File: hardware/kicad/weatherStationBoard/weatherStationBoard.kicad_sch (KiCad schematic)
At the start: 7 parts, among them P1 USB_C_Plug_USB2.0, SW1 SW_Push, SW2 SW_Push, U1 ESP-12F, U2 AMS1117, U3 CH340C

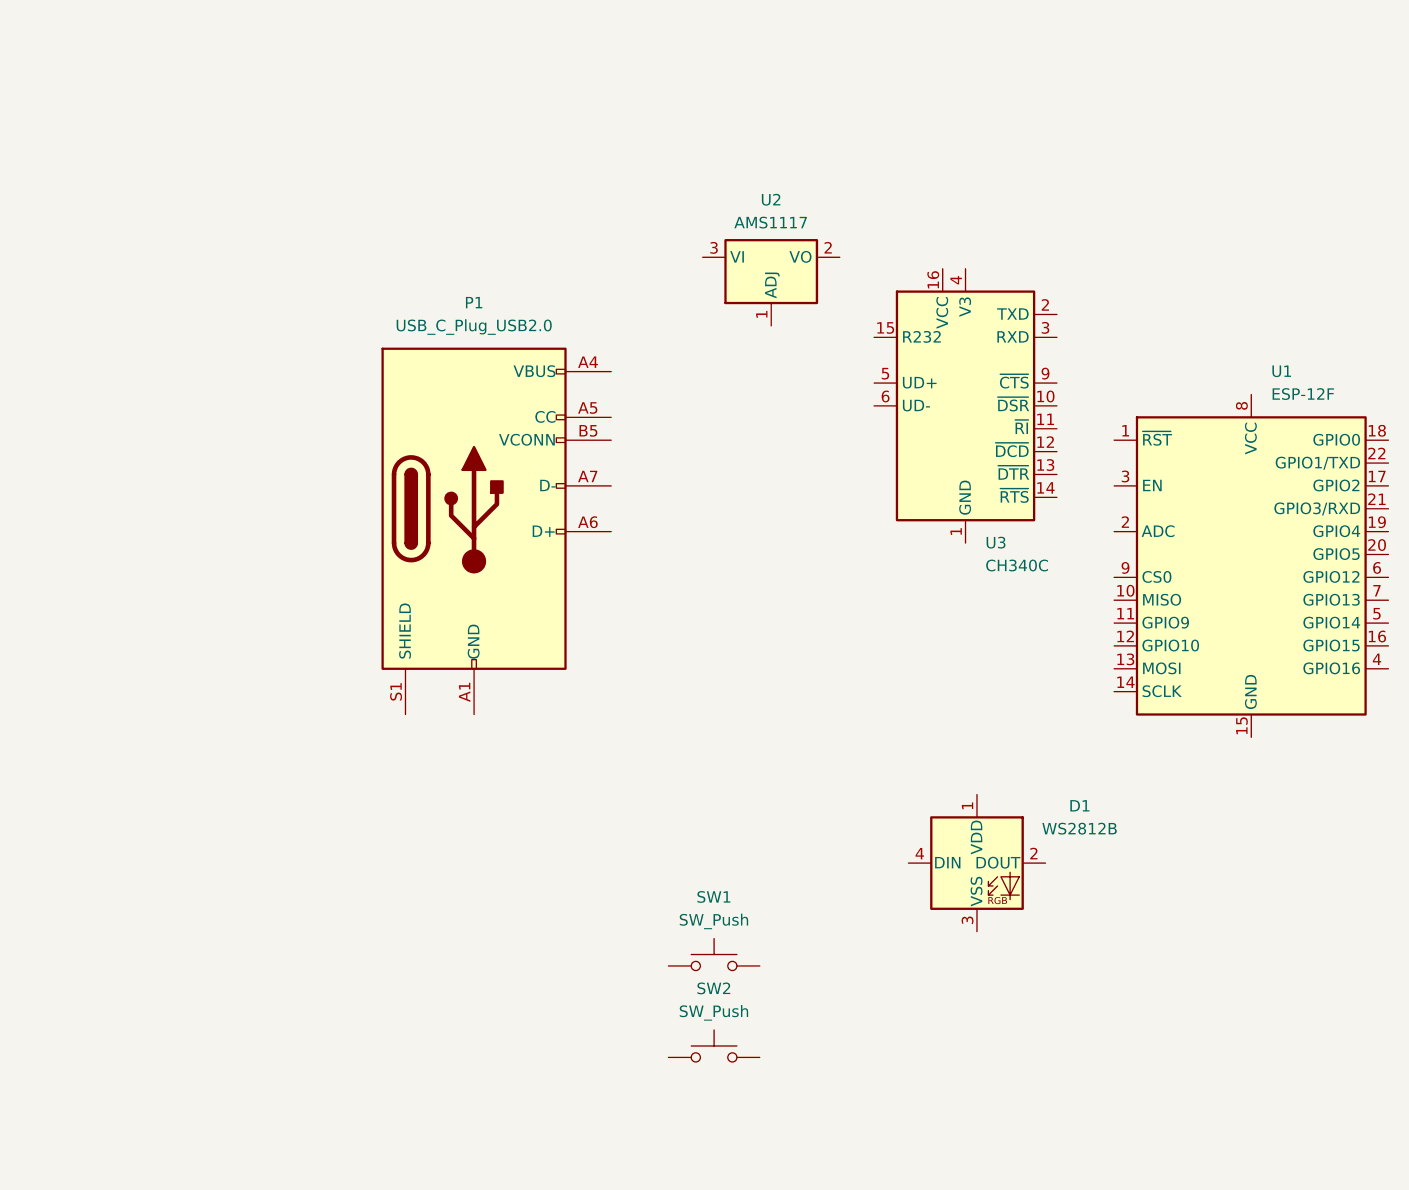
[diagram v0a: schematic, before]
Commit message: PCB Simple LED Circuit With Usb-C
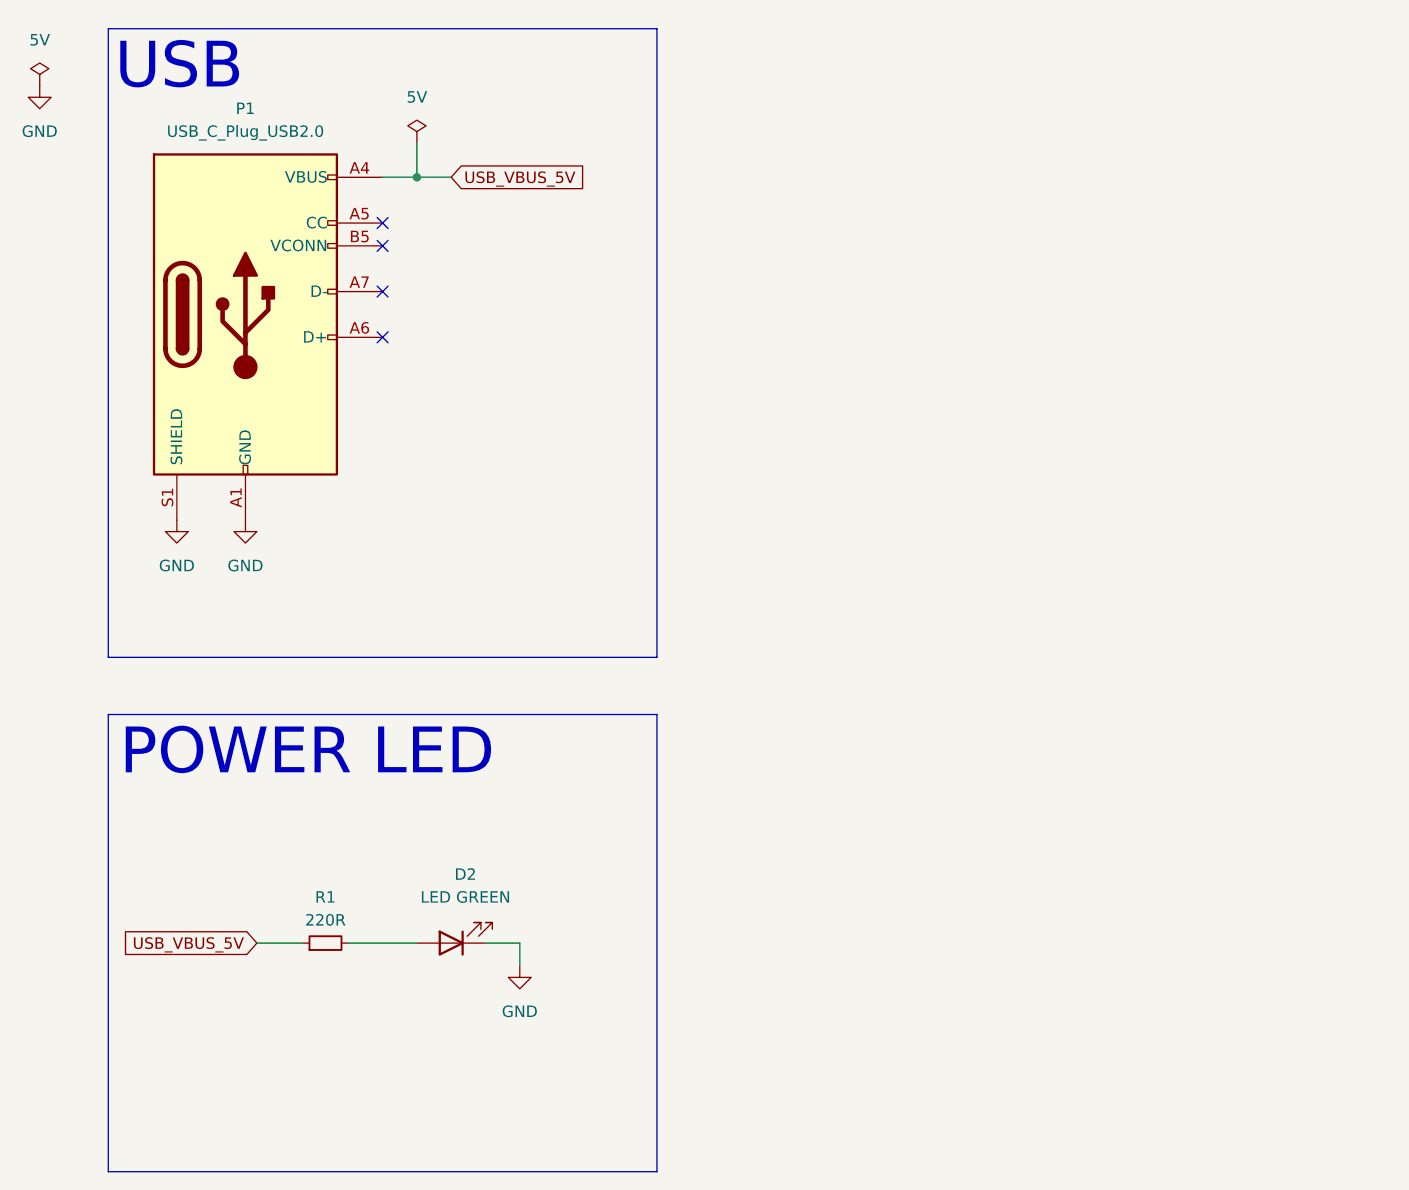
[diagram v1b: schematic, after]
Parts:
- removed D1: WS2812B, LED_SMD:LED_WS2812B_PLCC4_5.0x5.0mm_P3.2mm, symbol LED:WS2812B
- removed SW1, SW2: SW_Push, symbol Switch:SW_Push
- removed U1: ESP-12F, RF_Module:ESP-12E, symbol RF_Module:ESP-12F
- removed U2: AMS1117, Package_TO_SOT_SMD:SOT-223-3_TabPin2, symbol Regulator_Linear:AMS1117
- removed U3: CH340C, Package_SO:SOIC-16_3.9x9.9mm_P1.27mm, symbol Interface_USB:CH340C
- added D2: LED GREEN, LED_SMD:LED_0805_2012Metric, symbol Device:LED
- added R1: 220R, Resistor_SMD:R_0805_2012Metric, symbol Device:R_Small
- P1: footprint (none) -> Connector_USB:USB_C_Receptacle_GCT_USB4085
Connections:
- net GND: now reaches P1.A1 (GND), P1.A12 (GND), P1.B1 (GND), P1.B12 (GND)
- net GND: now also P1.S1 (SHIELD), D2.1 (K)
- net USB_VBUS_5V: now reaches P1.A4 (VBUS), P1.A9 (VBUS), P1.B4 (VBUS), P1.B9 (VBUS)
- net USB_VBUS_5V: now also R1.1
- new net: D2.2 (A), R1.2
- no-connect marks 0 -> 4
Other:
- note added: "POWER LED"
- note added: "USB"
- moved on the sheet: P1

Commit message: power, 5vto3v, usb to serial
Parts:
- added 12k1: R_Small, Resistor_SMD:R_0805_2012Metric, symbol Device:R_Small
- added C1, C10, C5, C6, C8: 100nF, Capacitor_SMD:C_0805_2012Metric, symbol Device:C_Small
- added C2, C7, C9: 10uF, Capacitor_SMD:C_0805_2012Metric, symbol Device:C_Small
- added C3, C4: 22pF, Capacitor_SMD:C_0805_2012Metric, symbol Device:C_Small
- added D1: LED, LED_SMD:LED_0805_2012Metric, symbol Device:LED_Small
- added Q1, Q2: S8050, Package_TO_SOT_THT:TO-92_Inline, symbol Transistor_BJT:S8050
- added R2, R3: 470R, Resistor_SMD:R_0805_2012Metric, symbol Device:R_Small
- added R4: 1k, Resistor_SMD:R_0805_2012Metric, symbol Device:R_Small
- added R5: 12k, Resistor_SMD:R_0805_2012Metric, symbol Device:R_Small
- added U1: ESP-12F, RF_Module:ESP-12E, symbol RF_Module:ESP-12F
- added U2: CH340G, Package_SO:SOIC-16_3.9x9.9mm_P1.27mm, symbol Interface_USB:CH340G
- added U4: AMS1117-3.3, Package_TO_SOT_SMD:SOT-223-3_TabPin2, symbol Regulator_Linear:AMS1117-3.3
- added Y1: Crystal_GND24_Small, Crystal:Crystal_SMD_3225-4Pin_3.2x2.5mm, symbol Device:Crystal_GND24_Small
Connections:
- net GND: now also C1.2, C10.2, C2.2, C3.2, C4.2, C5.2, C6.2, C7.2, C8.2, C9.2, D1.1 (K), U1.15 (GND), U2.1 (GND), U4.1 (GND), Y1.2, Y1.4
- net at P1.A6 (D+): now also U2.5 (UD+)
- net at P1.A7 (D-): now also U2.6 (UD-)
- net USB_VBUS_5V renamed 5V
- net 5V: now also C1.1, C2.1, C6.1, C7.1, U2.16 (VCC), U4.3 (VI)
- new net: R3.1, U2.3 (RXD)
- new net: D1.2 (A), R4.2
- new net: 12k1.1, Q2.2 (B)
- new net: R2.1, U2.2 (TXD)
- new net: Q1.2 (B), R5.1
- new net: C10.1, U2.4 (V3)
- new net 3V3: C5.1, C8.1, C9.1, R4.1, U1.8 (VCC), U4.2 (VO)
- new net DTR: 12k1.2, Q1.1 (E), U2.13 (~{DTR})
- new net ESP RX: R2.2, U1.21 (GPIO3/RXD)
- new net ESP TX: R3.2, U1.22 (GPIO1/TXD)
- new net GPIO0: Q1.3 (C), U1.18 (GPIO0)
- new net RTS: Q2.1 (E), R5.2, U2.14 (~{RTS})
- new net XI: C4.1, U2.7 (XI), Y1.3
- new net XO: C3.1, U2.8 (XO), Y1.1
- new net nRST: Q2.3 (C), U1.1 (~{RST})
- no-connect marks 4 -> 23
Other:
- note added: "5V 2 3V"
- note added: "Auto program circuit"
- note added: "ESP8266"
- moved on the sheet: D2, R1

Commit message: PCB updated
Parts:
- added R6: 5k1, Resistor_SMD:R_0805_2012Metric, symbol Device:R_Small
- Q1, Q2: footprint Package_TO_SOT_THT:TO-92_Inline -> Package_TO_SOT_SMD:SOT-23-3
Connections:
- net GND: now also R6.2
- net at P1.A5 (CC): now also R6.1
- no-connect marks 23 -> 22
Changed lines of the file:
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@@
 	)
 	(no_connect
-		(at 43.18 34.29)
-	)
-	(no_connect
 		(at 175.26 45.72)
 	)
@@
 	(wire
 		(pts
+			(xy 43.18 34.29) (xy 45.72 34.29)
+		)
+		(stroke
+			(width 0)
+			(type default)
+		)
+	)
+	(wire
+		(pts
 			(xy 63.5 57.15) (xy 66.04 57.15)
 		)
@@
 	(wire
 		(pts
+			(xy 50.8 34.29) (xy 53.34 34.29)
+		)
+		(stroke
+			(width 0)
+			(type default)
+		)
+	)
+	(wire
+		(pts
 			(xy 212.09 31.75) (xy 218.44 31.75)
 		)
@@
 	)
 	(symbol
+		(lib_id "Device:R_Small")
+		(at 48.26 34.29 90)
+		(unit 1)
+		(exclude_from_sim no)
+		(in_bom yes)
+		(on_board yes)
+		(dnp no)
+		(property "Reference" "R6"
+			(at 55.626 34.544 90)
+			(effects
+				(font
+					(size 1.27 1.27)
+				)
+			)
+		)
+		(property "Value" "5k1"
+			(at 48.26 36.83 90)
+			(effects
+				(font
+					(size 1.27 1.27)
+				)
+			)
+		)
+		(property "Footprint" "Resistor_SMD:R_0805_2012Metric"
+			(at 48.26 34.29 0)
+			(effects
+				(font
+					(size 1.27 1.27)
+				)
+				(hide yes)
+			)
+		)
+		(property "Datasheet" "~"
+			(at 48.26 34.29 0)
+			(effects
+				(font
+					(size 1.27 1.27)
+				)
+				(hide yes)
+			)
+		)
+		(property "Description" "Resistor, small symbol"
+			(at 48.26 34.29 0)
+			(effects
+				(font
+					(size 1.27 1.27)
+				)
+				(hide yes)
+			)
+		)
+		(pin "2"
+		)
+		(pin "1"
+		)
+		(instances
+			(project "weatherStationBoard"
+				(path "/8b822046-1d25-4aa8-8dbc-df598e1eff63"
+					(reference "R6")
+					(unit 1)
+				)
+			)
+		)
+	)
+	(symbol
 		(lib_id "power:GND")
 		(at 252.73 38.1 0)
@@
 			)
 		)
-		(property "Footprint" "Package_TO_SOT_THT:TO-92_Inline"
+		(property "Footprint" "Package_TO_SOT_SMD:SOT-23-3"
 			(at 73.66 102.235 0)
 			(effects
@@
 	)
 	(symbol
+		(lib_id "power:GND")
+		(at 53.34 34.29 0)
+		(unit 1)
+		(exclude_from_sim no)
+		(in_bom yes)
+		(on_board yes)
+		(dnp no)
+		(fields_autoplaced yes)
+		(property "Reference" "#PWR020"
+			(at 53.34 40.64 0)
+			(effects
+				(font
+					(size 1.27 1.27)
+				)
+				(hide yes)
+			)
+		)
+		(property "Value" "GND"
+			(at 53.34 39.37 0)
+			(effects
+				(font
+					(size 1.27 1.27)
+				)
+			)
+		)
+		(property "Footprint" ""
+			(at 53.34 34.29 0)
+			(effects
+				(font
+					(size 1.27 1.27)
+				)
+				(hide yes)
+			)
+		)
+		(property "Datasheet" ""
+			(at 53.34 34.29 0)
+			(effects
+				(font
+					(size 1.27 1.27)
+				)
+				(hide yes)
+			)
+		)
+		(property "Description" "Power symbol creates a global label with name \"GND\" , ground"
+			(at 53.34 34.29 0)
+			(effects
+				(font
+					(size 1.27 1.27)
+				)
+				(hide yes)
+			)
+		)
+		(pin "1"
+		)
+		(instances
+			(project "weatherStationBoard"
+				(path "/8b822046-1d25-4aa8-8dbc-df598e1eff63"
+					(reference "#PWR020")
+					(unit 1)
+				)
+			)
+		)
+	)
+	(symbol
 		(lib_id "Device:R_Small")
 		(at 91.44 115.57 90)
@@
 			)
 		)
-		(property "Footprint" "Package_TO_SOT_THT:TO-92_Inline"
+		(property "Footprint" "Package_TO_SOT_SMD:SOT-23-3"
 			(at 73.66 113.665 0)
 			(effects

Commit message: Pushbutton files
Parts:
- added R7: 10k, Resistor_SMD:R_0805_2012Metric, symbol Device:R_Small
- added SW1: SW_Push, symbol Switch:SW_Push
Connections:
- net 3V3: now also R7.2
- net nRST: now also R7.1, SW1.1
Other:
- note added: "RESET"
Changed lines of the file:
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@@
 	(generator "eeschema")
 	(generator_version "8.0")
-	(paper "A4")
+	(paper "A3")
 	(junction
 		(at 63.5 29.21)
@@
 	)
 	(junction
+		(at 134.62 109.22)
+		(diameter 0)
+		(color 0 0 0 0)
+	)
+	(junction
 		(at 252.73 24.13)
 		(diameter 0)
@@
 	(wire
 		(pts
+			(xy 134.62 106.68) (xy 134.62 109.22)
+		)
+		(stroke
+			(width 0)
+			(type default)
+		)
+	)
+	(wire
+		(pts
 			(xy 63.5 29.21) (xy 68.58 29.21)
 		)
@@
 	(wire
 		(pts
+			(xy 134.62 109.22) (xy 140.97 109.22)
+		)
+		(stroke
+			(width 0)
+			(type default)
+		)
+	)
+	(wire
+		(pts
+			(xy 134.62 97.79) (xy 134.62 101.6)
+		)
+		(stroke
+			(width 0)
+			(type default)
+		)
+	)
+	(wire
+		(pts
 			(xy 252.73 36.83) (xy 252.73 38.1)
 		)
@@
 	(wire
 		(pts
+			(xy 134.62 109.22) (xy 134.62 113.03)
+		)
+		(stroke
+			(width 0)
+			(type default)
+		)
+	)
+	(wire
+		(pts
 			(xy 45.72 68.58) (xy 45.72 63.5)
 		)
@@
 	)
 	(rectangle
+		(start 120.65 83.82)
+		(end 172.72 134.62)
+		(stroke
+			(width 0)
+			(type default)
+		)
+		(fill
+			(type none)
+		)
+	)
+	(rectangle
 		(start 59.69 83.82)
 		(end 118.11 134.62)
@@
 		)
 	)
+	(text "RESET\n"
+		(exclude_from_sim no)
+		(at 132.588 88.392 0)
+		(effects
+			(font
+				(size 5.08 5.08)
+			)
+		)
+	)
 	(text "ESP8266"
 		(exclude_from_sim no)
@@
 		)
 	)
+	(label "nRST"
+		(at 140.97 109.22 0)
+		(fields_autoplaced yes)
+		(effects
+			(font
+				(size 1.27 1.27)
+			)
+			(justify left bottom)
+		)
+	)
 	(label "ESP TX"
 		(at 184.15 35.56 0)
@@
 	(global_label "3V3"
 		(shape input)
+		(at 134.62 97.79 90)
+		(fields_autoplaced yes)
+		(effects
+			(font
+				(size 1.27 1.27)
+			)
+			(justify left)
+		)
+		(property "Intersheetrefs" "${INTERSHEET_REFS}"
+			(at 134.62 91.2972 90)
+			(effects
+				(font
+					(size 1.27 1.27)
+				)
+				(justify left)
+				(hide yes)
+			)
+		)
+	)
+	(global_label "3V3"
+		(shape input)
 		(at 262.89 24.13 0)
 		(fields_autoplaced yes)
@@
 	)
 	(symbol
+		(lib_id "Switch:SW_Push")
+		(at 134.62 118.11 270)
+		(unit 1)
+		(exclude_from_sim no)
+		(in_bom yes)
+		(on_board yes)
+		(dnp no)
+		(fields_autoplaced yes)
+		(property "Reference" "SW1"
+			(at 138.43 116.8399 90)
+			(effects
+				(font
+					(size 1.27 1.27)
+				)
+				(justify left)
+			)
+		)
+		(property "Value" "SW_Push"
+			(at 138.43 119.3799 90)
+			(effects
+				(font
+					(size 1.27 1.27)
+				)
+				(justify left)
+			)
+		)
+		(property "Footprint" ""
+			(at 139.7 118.11 0)
+			(effects
+				(font
+					(size 1.27 1.27)
+				)
+				(hide yes)
+			)
+		)
+		(property "Datasheet" "~"
+			(at 139.7 118.11 0)
+			(effects
+				(font
+					(size 1.27 1.27)
+				)
+				(hide yes)
+			)
+		)
+		(property "Description" "Push button switch, generic, two pins"
+			(at 134.62 118.11 0)
+			(effects
+				(font
+					(size 1.27 1.27)
+				)
+				(hide yes)
+			)
+		)
+		(pin "1"
+		)
+		(pin "2"
+		)
+		(instances
+			(project ""
+				(path "/8b822046-1d25-4aa8-8dbc-df598e1eff63"
+					(reference "SW1")
+					(unit 1)
+				)
+			)
+		)
+	)
+	(symbol
 		(lib_id "power:GND")
 		(at 236.22 38.1 0)
@@
 					(unit 1)
 				)
+			)
+		)
+	)
+	(symbol
+		(lib_id "Device:R_Small")
+		(at 134.62 104.14 180)
+		(unit 1)
+		(exclude_from_sim no)
+		(in_bom yes)
+		(on_board yes)
+		(dnp no)
+		(property "Reference" "R7"
+			(at 130.81 103.378 0)
+			(effects
+				(font
+					(size 1.27 1.27)
+				)
+			)
+		)
+		(property "Value" "10k"
+			(at 130.81 105.918 0)
+			(effects
+				(font
+					(size 1.27 1.27)
+				)
+			)
+		)
+		(property "Footprint" "Resistor_SMD:R_0805_2012Metric"
+			(at 134.62 104.14 0)
+			(effects
+				(font
+					(size 1.27 1.27)
+				)
+				(hide yes)
+			)
+		)
+		(property "Datasheet" "~"
+			(at 134.62 104.14 0)
+			(effects
+				(font
+					(size 1.27 1.27)
+				)
+				(hide yes)
+			)
+		)
+		(property "Description" "Resistor, small symbol"
+			(at 134.62 104.14 0)
+			(effects
+				(font
+					(size 1.27 1.27)
+				)
+				(hide yes)
+			)
+		)
+		(pin "1"
+		)
+		(pin "2"
+		)
+		(instances
+			(project "weatherStationBoard"
+				(path "/8b822046-1d25-4aa8-8dbc-df598e1eff63"
+					(reference "R7")
+					(unit 1)
+				)

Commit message: Updated usb connector
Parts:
- added S1: PTS645SM43SMTR92LFS, PTS645SM43SMTR92LFS:PTS645_SMT_, symbol PTS645SM43SMTR92LFS:PTS645SM43SMTR92LFS
- P1: footprint Connector_USB:USB_C_Receptacle_GCT_USB4085 -> Connector_USB:USB_C_Receptacle_XKB_U262-16XN-4BVC11
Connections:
- no-connect marks 22 -> 27
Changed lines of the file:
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@@
+	)
+	(no_connect
+		(at 134.62 123.19)
+	)
+	(no_connect
+		(at 148.59 121.92)
 	)
 	(no_connect
@@
 	)
 	(no_connect
+		(at 148.59 124.46)
+	)
+	(no_connect
 		(at 144.78 48.26)
 	)
@@
 	)
 	(no_connect
+		(at 168.91 121.92)
+	)
+	(no_connect
 		(at 144.78 38.1)
 	)
@@
 	(no_connect
 		(at 144.78 53.34)
+	)
+	(no_connect
+		(at 168.91 124.46)
 	)
 	(no_connect
@@
 	)
 	(symbol
+		(lib_id "PTS645SM43SMTR92LFS:PTS645SM43SMTR92LFS")
+		(at 148.59 121.92 0)
+		(unit 1)
+		(exclude_from_sim no)
+		(in_bom yes)
+		(on_board yes)
+		(dnp no)
+		(fields_autoplaced yes)
+		(property "Reference" "S1"
+			(at 158.75 114.3 0)
+			(effects
+				(font
+					(size 1.27 1.27)
+				)
+			)
+		)
+		(property "Value" "PTS645SM43SMTR92LFS"
+			(at 158.75 116.84 0)
+			(effects
+				(font
+					(size 1.27 1.27)
+				)
+			)
+		)
+		(property "Footprint" "PTS645SM43SMTR92LFS:PTS645_SMT_"
+			(at 165.1 119.38 0)
+			(effects
+				(font
+					(size 1.27 1.27)
+				)
+				(justify left)
+				(hide yes)
+			)
+		)
+		(property "Datasheet" "https://www.ckswitches.com/media/1471/pts645.pdf"
+			(at 165.1 121.92 0)
+			(effects
+				(font
+					(size 1.27 1.27)
+				)
+				(justify left)
+				(hide yes)
+			)
+		)
+		(property "Description" "C & K COMPONENTS - PTS645SM43SMTR92LFS - SWITCH, SPST, 0.05A, 12VDC, SMD, 4.3MM"
+			(at 148.59 121.92 0)
+			(effects
+				(font
+					(size 1.27 1.27)
+				)
+				(hide yes)
+			)
+		)
+		(property "Description_1" "C & K COMPONENTS - PTS645SM43SMTR92LFS - SWITCH, SPST, 0.05A, 12VDC, SMD, 4.3MM"
+			(at 165.1 124.46 0)
+			(effects
+				(font
+					(size 1.27 1.27)
+				)
+				(justify left)
+				(hide yes)
+			)
+		)
+		(property "Height" ""
+			(at 165.1 127 0)
+			(effects
+				(font
+					(size 1.27 1.27)
+				)
+				(justify left)
+				(hide yes)
+			)
+		)
+		(property "Manufacturer_Name" "C & K COMPONENTS"
+			(at 165.1 129.54 0)
+			(effects
+				(font
+					(size 1.27 1.27)
+				)
+				(justify left)
+				(hide yes)
+			)
+		)
+		(property "Manufacturer_Part_Number" "PTS645SM43SMTR92LFS"
+			(at 165.1 132.08 0)
+			(effects
+				(font
+					(size 1.27 1.27)
+				)
+				(justify left)
+				(hide yes)
+			)
+		)
+		(property "Mouser Part Number" "611-PTS645SM43SMTR92"
+			(at 165.1 134.62 0)
+			(effects
+				(font
+					(size 1.27 1.27)
+				)
+				(justify left)
+				(hide yes)
+			)
+		)
+		(property "Mouser Price/Stock" "https://www.mouser.co.uk/ProductDetail/CK/PTS645SM43SMTR92LFS?qs=FESYatJ8odKPktxv6ncfWg%3D%3D"
+			(at 165.1 137.16 0)
+			(effects
+				(font
+					(size 1.27 1.27)
+				)
+				(justify left)
+				(hide yes)
+			)
+		)
+		(property "Arrow Part Number" "PTS645SM43SMTR92LFS"
+			(at 165.1 139.7 0)
+			(effects
+				(font
+					(size 1.27 1.27)
+				)
+				(justify left)
+				(hide yes)
+			)
+		)
+		(property "Arrow Price/Stock" "https://www.arrow.com/en/products/pts645sm43smtr92lfs/ck"
+			(at 165.1 142.24 0)
+			(effects
+				(font
+					(size 1.27 1.27)
+				)
+				(justify left)
+				(hide yes)
+			)
+		)
+		(pin "1"
+		)
+		(pin "2"
+		)
+		(pin "4"
+		)
+		(pin "3"
+		)
+		(instances
+			(project ""
+				(path "/8b822046-1d25-4aa8-8dbc-df598e1eff63"
+					(reference "S1")
+					(unit 1)
+				)
+			)
+		)
+	)
+	(symbol
 		(lib_id "power:GND")
 		(at 20.32 67.31 0)
@@
 			)
 		)
-		(property "Footprint" "Connector_USB:USB_C_Receptacle_GCT_USB4085"
+		(property "Footprint" "Connector_USB:USB_C_Receptacle_XKB_U262-16XN-4BVC11"
 			(at 31.75 44.45 0)
 			(effects

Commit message: board design prototype no periphery
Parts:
- removed 12k1: R_Small, Resistor_SMD:R_0805_2012Metric, symbol Device:R_Small
- removed P1: USB_C_Plug_USB2.0, Connector_USB:USB_C_Receptacle_XKB_U262-16XN-4BVC11, symbol Connector:USB_C_Plug_USB2.0
- removed SW1: SW_Push, symbol Switch:SW_Push
- added J1: USB_C_Receptacle_USB2.0_16P, Connector_USB:USB_C_Receptacle_XKB_U262-16XN-4BVC11, symbol Connector:USB_C_Receptacle_USB2.0_16P
- added R8: 5k1, Resistor_SMD:R_0805_2012Metric, symbol Device:R_Small
- added R9: 12k, Resistor_SMD:R_0805_2012Metric, symbol Device:R_Small
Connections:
- net 5V: now also J1.A4 (VBUS), J1.A9 (VBUS), J1.B4 (VBUS), J1.B9 (VBUS)
- net DTR: now also R9.2
- net GND: now also S1.3, J1.A1 (GND), J1.A12 (GND), J1.B1 (GND), J1.B12 (GND), J1.S1 (SHIELD), R8.2
- net nRST: now also S1.1
- net at R6.1: now also J1.A5 (CC1)
- net at U2.5 (UD+): now also J1.A6 (D+), J1.B6 (D+)
- net at U2.6 (UD-): now also J1.A7 (D-), J1.B7 (D-)
- net at Q2.2 (B): now also R9.1
- new net: J1.B5 (CC2), R8.1
- no-connect marks 27 -> 25
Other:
- moved on the sheet: S1
